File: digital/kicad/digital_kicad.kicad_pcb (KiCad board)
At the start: 2 copper layers, 93 x 49.5 mm, 23 parts, among them J1 Barrel_Jack_Switch, J2 Screw_Terminal_01x02, Q1 2N3904, Q2 2N3904, Q3 FDN340P, Q4 2N3904, SW1 SW_SPST

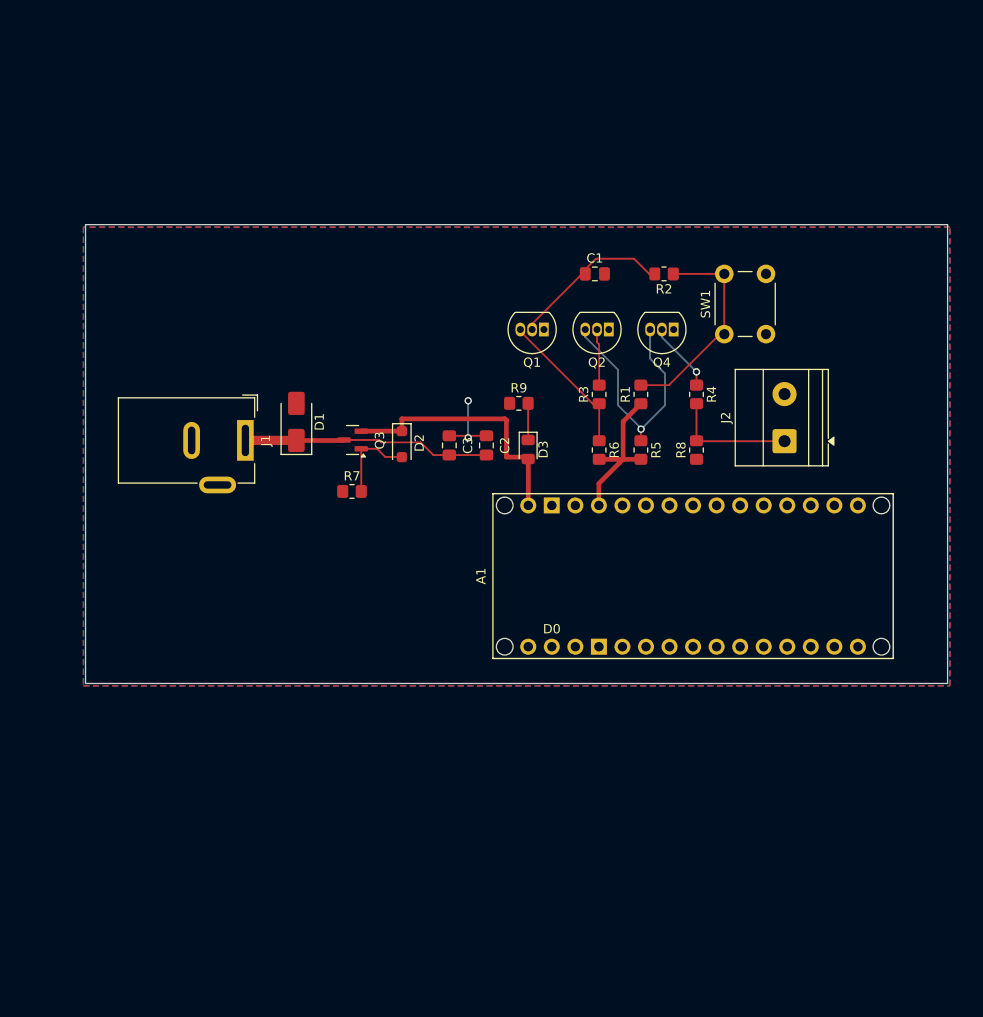
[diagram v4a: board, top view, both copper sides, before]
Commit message: redid the digital schematic to be more compact
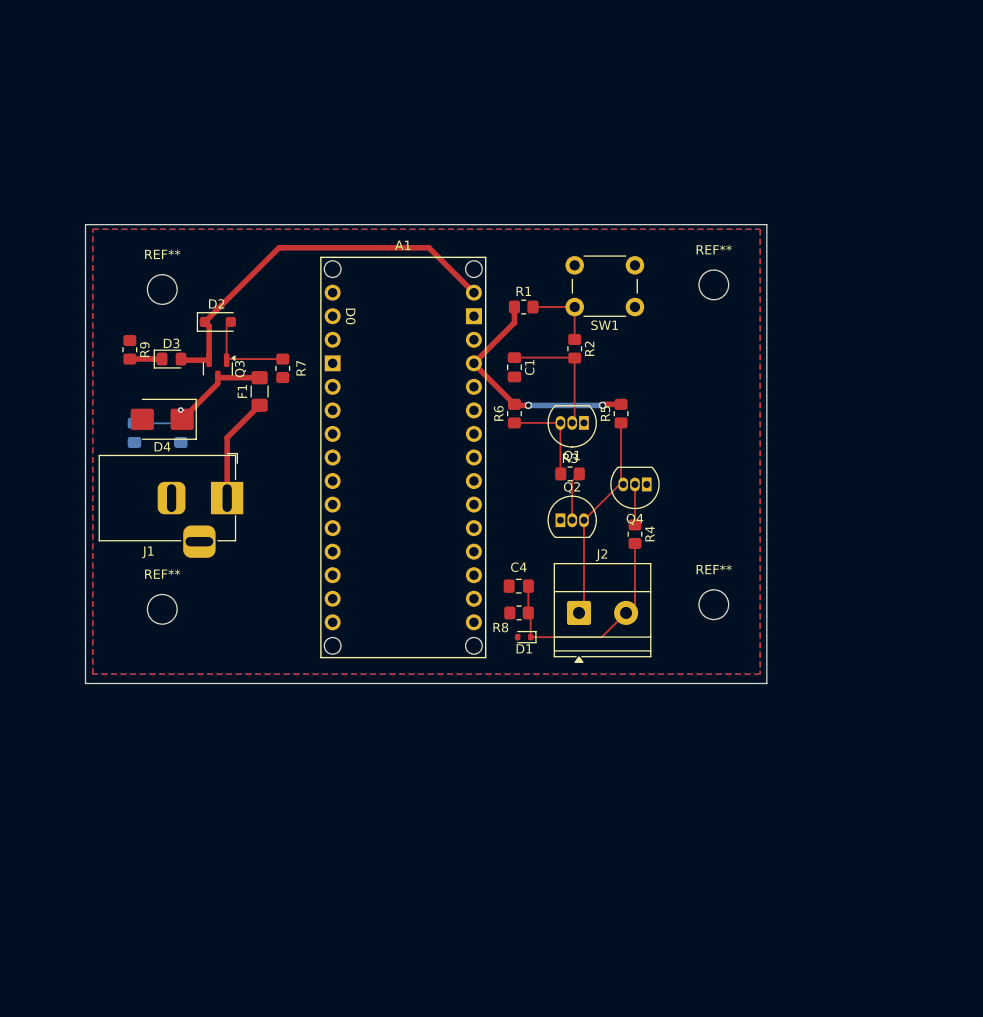
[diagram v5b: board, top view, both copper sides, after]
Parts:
- added C4: 1u, Capacitor_SMD:C_0805_2012Metric_Pad1.18x1.45mm_HandSolder, F.Cu at (152.0, 84.5)
- added D4: SM6T18A, Diode_SMD:D_SMB, F.Cu at (113.5, 66.5)
- added F1: Polyfuse, Fuse:Fuse_1206_3216Metric_Pad1.42x1.75mm_HandSolder, F.Cu at (124.0, 63.5)
- added REF**: MountingHole_3.2mm_M3_DIN965, MountingHole:MountingHole_3.2mm_M3_DIN965, F.Cu at (113.5, 87.0)
- added REF**: MountingHole_3.2mm_M3_DIN965, MountingHole:MountingHole_3.2mm_M3_DIN965, F.Cu at (113.5, 52.5)
- added REF**: MountingHole_3.2mm_M3_DIN965, MountingHole:MountingHole_3.2mm_M3_DIN965, F.Cu at (173.0, 52.0)
- added REF**: MountingHole_3.2mm_M3_DIN965, MountingHole:MountingHole_3.2mm_M3_DIN965, F.Cu at (173.0, 86.5)
- C2, C3: moved to B.Cu
- D1: value SMAJ13A -> ESD5Zxx; footprint Diode_SMD:D_SMA -> Diode_SMD:D_SOD-523
- J1: footprint Connector_BarrelJack:BarrelJack_Wuerth_6941xx301002 -> Connector_BarrelJack:BarrelJack_Horizontal
- R7: value 100k -> 10k
- moved A1 53.6 mm to (139.5, 92.2), turned to 0 degrees
- moved R9 42.4 mm to (110.0, 59.0), turned to -90 degrees
- moved D3 39.7 mm to (114.5, 60.0), turned to 0 degrees
- moved C3 34.0 mm to (110.5, 68.0), turned to -90 degrees
- moved D1 33.8 mm to (152.5, 90.0), turned to 180 degrees
- moved C2 33.0 mm to (115.5, 68.0), turned to -90 degrees
- moved J2 28.9 mm to (158.5, 87.4), turned to 0 degrees
- moved R8 26.0 mm to (152.0, 87.4), turned to 0 degrees
- moved D2 23.8 mm to (119.5, 56.0), turned to 0 degrees
- moved Q2 21.2 mm to (156.5, 77.4), turned to 0 degrees
- moved Q4 17.0 mm to (165.8, 73.5)
- moved R4 16.5 mm to (164.5, 78.9)
- moved Q3 16.4 mm to (119.5, 61.1), turned to -90 degrees
- moved R1 15.8 mm to (152.5, 54.4), turned to 0 degrees
- moved R7 15.2 mm to (126.5, 61.0), turned to 90 degrees
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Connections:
- C2 pad 1: Net-(D1-A1) -> Net-(D4-A1)
- C3 pad 1: Net-(D1-A1) -> Net-(D4-A1)
- D1 pad 1: Net-(D1-A1) -> /DIG_IN
- J1 pad 1: Net-(D1-A1) -> Net-(F1-Pad1)
- J2 pad 1: /DIG_IN -> /OUT
- J2 pad 2: unconnected-(J2-Pin_2-Pad2) -> /DIG_IN
- Q3 pad 3: Net-(D1-A1) -> Net-(D4-A1)
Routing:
- net Net-(D1-A1): track 26.7 -> 0.00 mm
- net Net-(D4-A1): track 0.00 -> 18.1 mm, vias 0 -> 1
- net /SW: track 23.3 -> 8.00 mm
- net /VDC: track 28.6 -> 41.7 mm
- net Net-(F1-Pad1): track 0.00 -> 11.5 mm
- net /DIG_IN: track 13.5 -> 24.9 mm
- net +5V: track 17.4 -> 25.7 mm, vias 0 -> 2
- net GND: track 8.18 -> 0.00 mm, vias 2 -> 0
- net /inv. SW: track 15.9 -> 10.5 mm
- net /OUT: track 27.0 -> 22.8 mm, vias 1 -> 0
- net Net-(Q1-B): track 17.7 -> 13.6 mm
- net A: track 7.55 -> 4.36 mm, vias 1 -> 0
- net Net-(D2-A): track 9.35 -> 10.4 mm
- net Net-(Q2-B): track 6.10 -> 5.32 mm
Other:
- board size 93 x 49.5 mm -> 73.5 x 49.5 mm

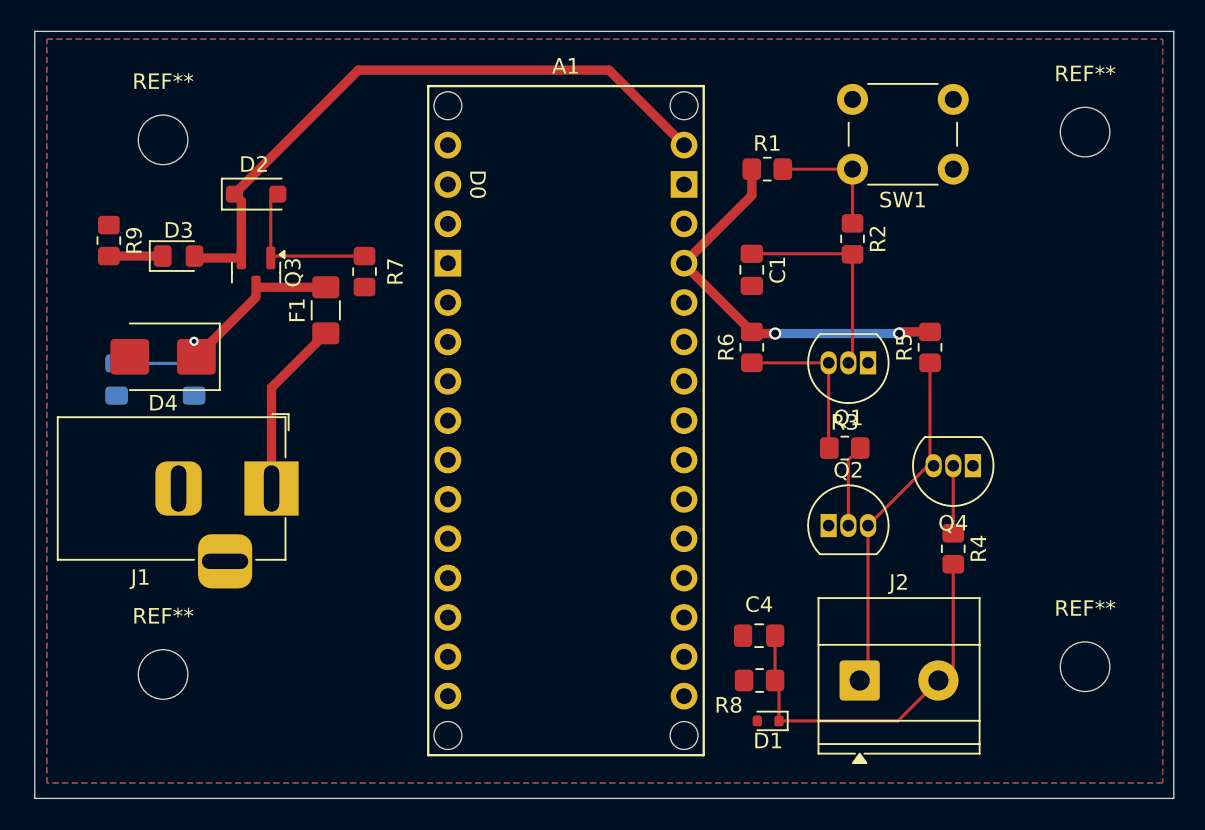
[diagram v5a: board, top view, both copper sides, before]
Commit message: fixed pcb silkscreen, added power switch
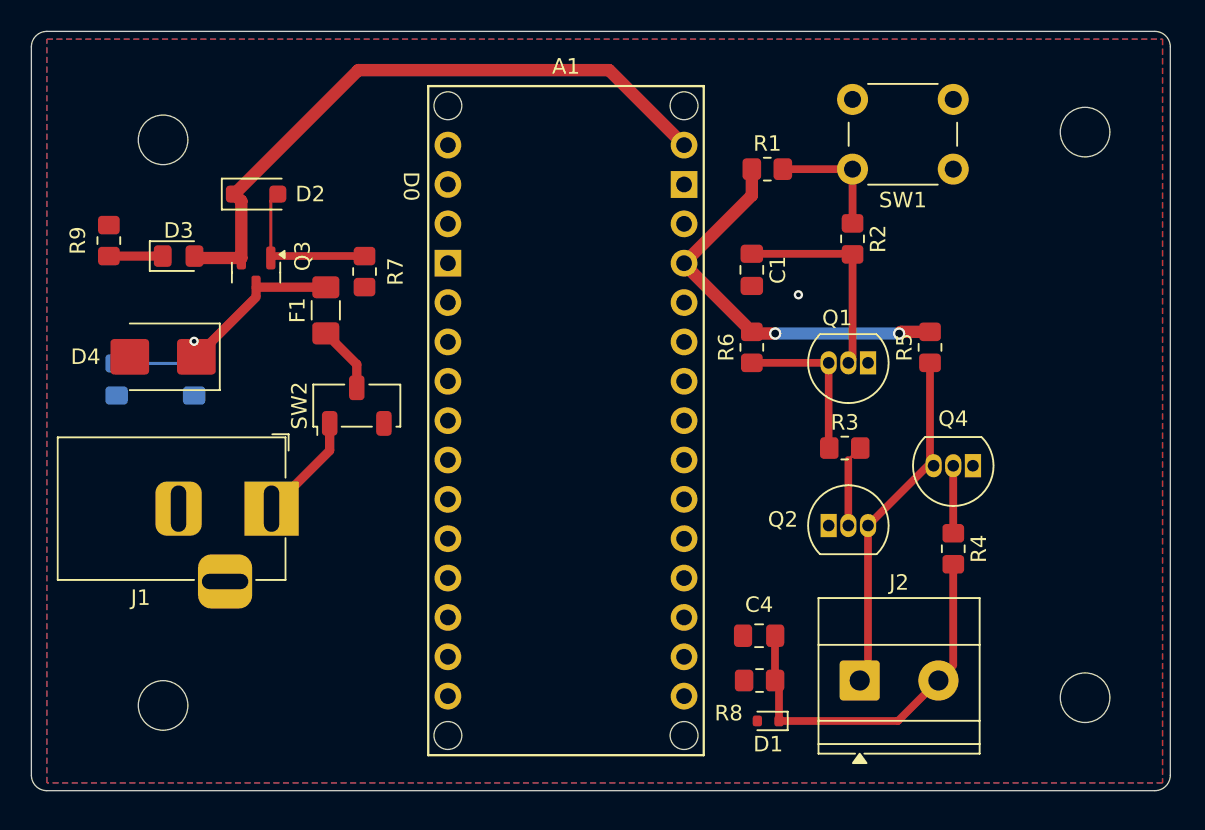
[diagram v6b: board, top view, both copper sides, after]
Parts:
- added SW2: SW_Nidec_CAS-120A1, Button_Switch_SMD:Nidec_Copal_CAS-120A, F.Cu at (126.0, 69.7)
- moved REF** 2.00 mm to (113.5, 89.0)
- moved REF** 2.00 mm to (173.0, 88.5)
- moved J1 1.30 mm to (120.5, 76.3)
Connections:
- F1 pad 1: Net-(F1-Pad1) -> Net-(SW2-B)
- J1 pad 1: Net-(F1-Pad1) -> Net-(SW2-C)
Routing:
- net Net-(F1-Pad1): track 11.5 -> 0.00 mm
- net Net-(SW2-C): track 0.00 -> 7.05 mm
- net Net-(SW2-B): track 0.00 -> 4.34 mm
- net GND: vias 0 -> 1
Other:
- board size 73.5 x 49.5 mm -> 73.5 x 49 mm

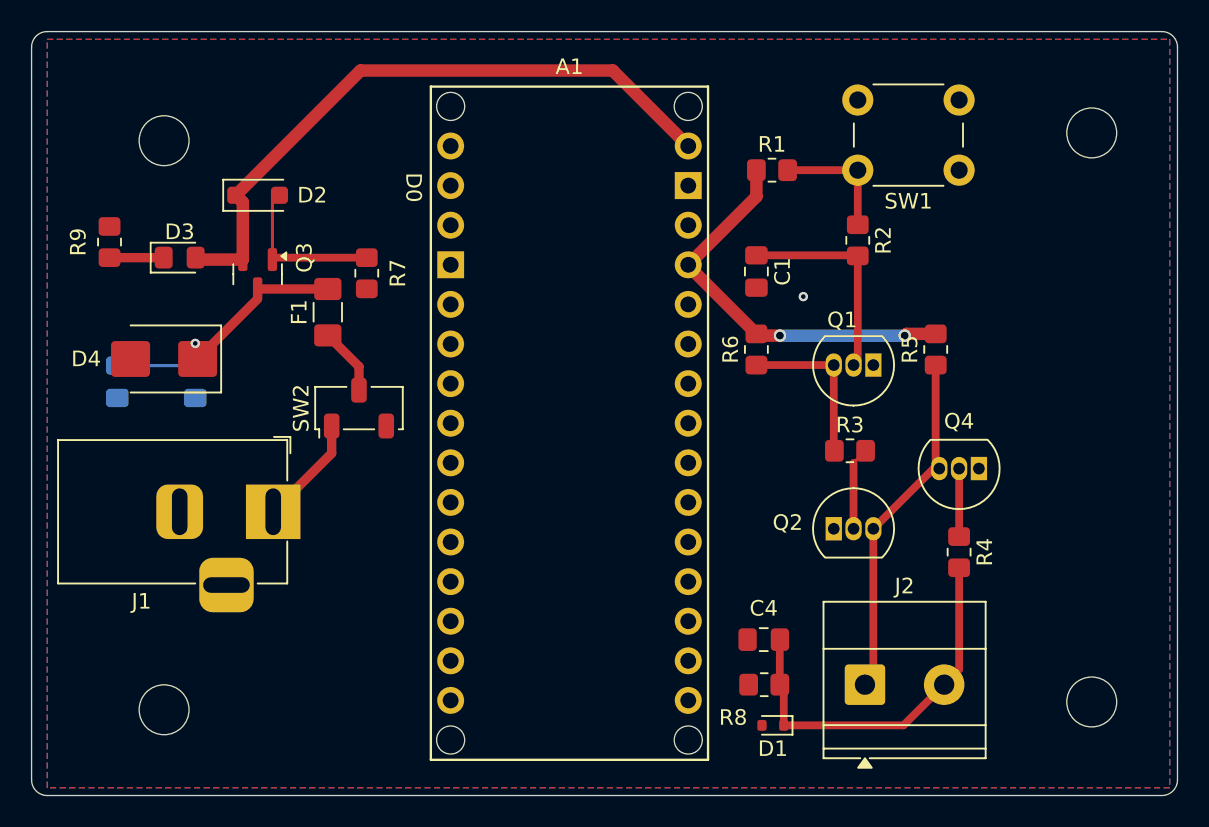
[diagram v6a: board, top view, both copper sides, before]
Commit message: added bigger switch, slightly improved the NOR pcb circuit side track routing
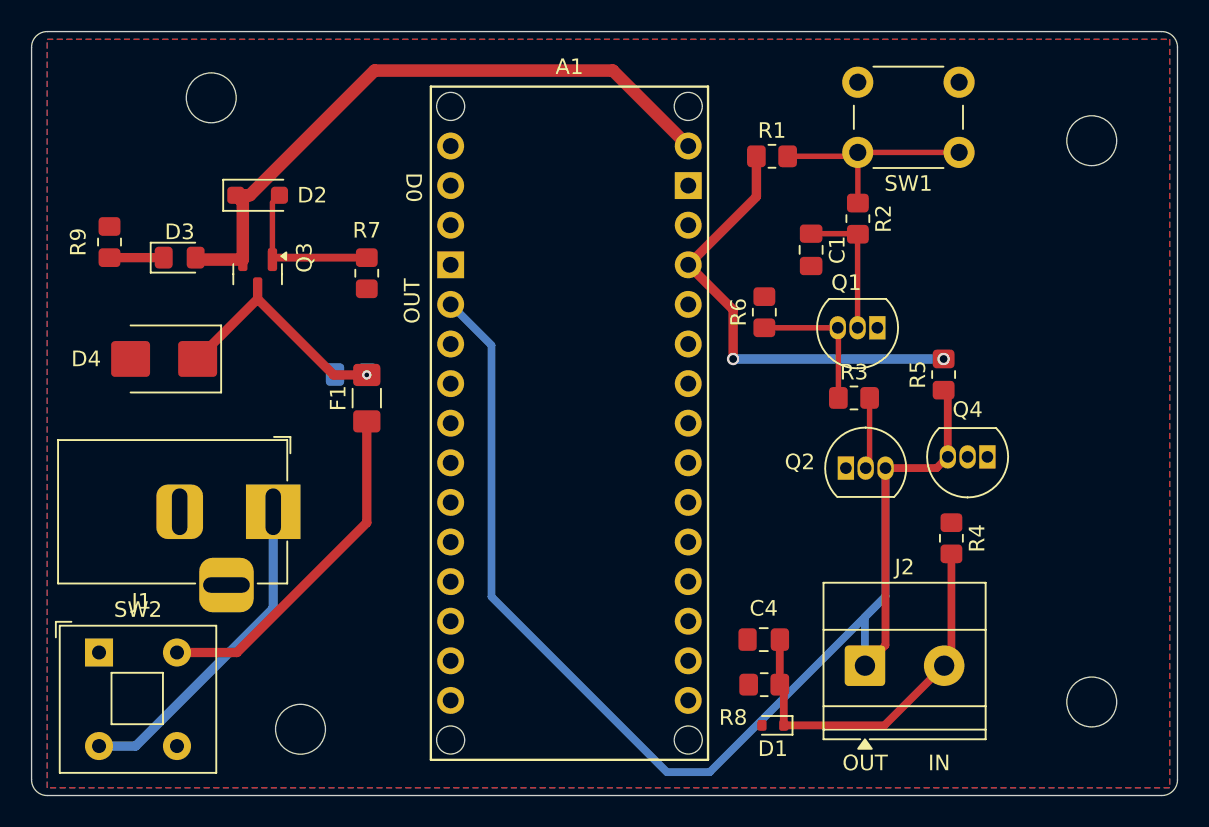
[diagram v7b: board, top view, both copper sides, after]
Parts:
- removed C3: 1u, Capacitor_SMD:C_0805_2012Metric_Pad1.18x1.45mm_HandSolder
- SW2: value SW_Nidec_CAS-120A1 -> SW_Push_SPDT; footprint Button_Switch_SMD:Nidec_Copal_CAS-120A -> Button_Switch_THT:SW_Push_2P1T_Toggle_CK_PVA1xxH1xxxxxxV2
- moved SW2 22.9 mm to (109.3, 85.3), turned to 0 degrees
- moved C2 10.0 mm to (125.5, 67.5), turned to 180 degrees
- moved REF** 8.84 mm to (122.2, 90.2)
- moved F1 6.05 mm to (126.5, 69.0)
- moved REF** 4.09 mm to (116.5, 49.8)
- moved Q2 3.97 mm to (157.2, 73.5)
- moved C1 3.77 mm to (155.0, 59.5)
- moved R3 3.40 mm to (157.8, 69.0)
- moved R6 2.44 mm to (152.0, 63.5)
- moved Q1 2.40 mm to (159.2, 64.5)
- moved R5 1.69 mm to (163.5, 67.5)
- moved R2 1.39 mm to (158.0, 57.5)
- moved J2 1.22 mm to (158.5, 86.2)
- moved SW1 1.14 mm to (164.5, 53.2)
- moved R4 1.02 mm to (164.0, 78.0)
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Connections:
- A1 pad D2: unconnected-(A1-D2_INT0-PadD2) -> /OUT
- SW2 pad 1: Net-(SW2-C) -> GND
- SW2 pad 3: GND -> Net-(SW2-C)
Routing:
- net /OUT: track 22.8 -> 89.2 mm
- net Net-(SW2-B): track 4.34 -> 22.1 mm
- net Net-(SW2-C): track 7.05 -> 21.0 mm
- net /SW: track 8.00 -> 14.0 mm
- net Net-(Q1-B): track 13.6 -> 8.94 mm
- net A: track 4.36 -> 0.00 mm
- net +5V: track 25.7 -> 29.5 mm
- net Net-(D4-A1): track 18.1 -> 15.1 mm
- net /inv. SW: track 10.5 -> 9.17 mm
- net /DIG_IN: track 24.9 -> 23.7 mm
- net Net-(Q2-B): track 5.32 -> 4.25 mm
- net GND: vias 1 -> 0
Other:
- board text added: "IN"
- board text added: "OUT"

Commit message: redid digital schematic to function as adapter, without arduino
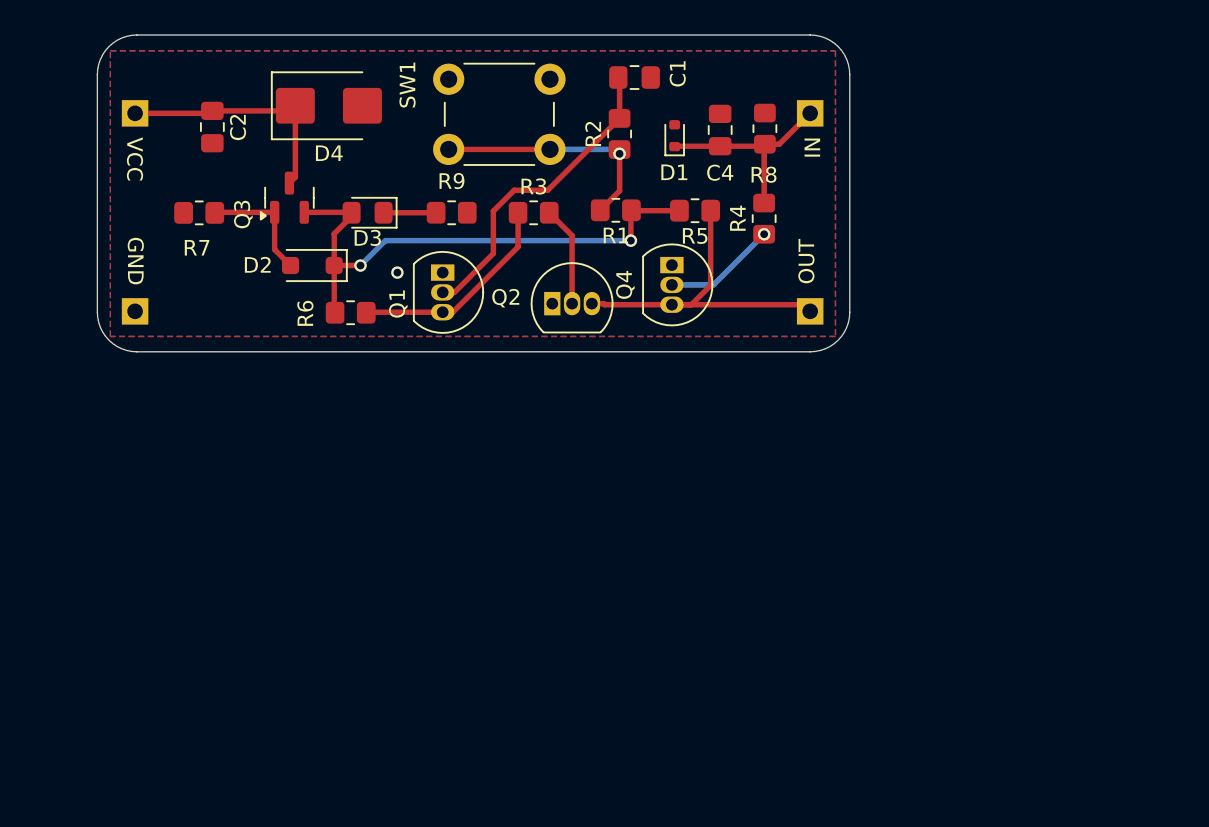
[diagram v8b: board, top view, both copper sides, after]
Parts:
- removed A1: Arduino_Nano_Socket, PCM_arduino-library:Arduino_Nano_Socket
- removed F1: Polyfuse, Fuse:Fuse_1206_3216Metric_Pad1.42x1.75mm_HandSolder
- removed REF** (x4): MountingHole_3.2mm_M3_DIN965, MountingHole:MountingHole_3.2mm_M3_DIN965
- removed SW2: SW_Push_SPDT, Button_Switch_THT:SW_Push_2P1T_Toggle_CK_PVA1xxH1xxxxxxV2
- added J3: Conn_01x01_Pin, Connector_PinHeader_2.54mm:PinHeader_1x01_P2.54mm_Vertical, B.Cu at (154.9, 63.4)
- added J4: Conn_01x01_Pin, Connector_PinHeader_2.54mm:PinHeader_1x01_P2.54mm_Vertical, B.Cu at (154.9, 50.7)
- C2: moved to F.Cu
- J1: value Barrel_Jack_Switch -> Conn_01x01_Pin; footprint Connector_BarrelJack:BarrelJack_Horizontal -> Connector_PinHeader_2.54mm:PinHeader_1x01_P2.54mm_Vertical; moved to B.Cu
- J2: value Screw_Terminal_01x02 -> Conn_01x01_Pin; footprint TerminalBlock_Phoenix:TerminalBlock_Phoenix_MKDS-1,5-2-5.08_1x02_P5.08mm_Horizontal -> Connector_PinHeader_2.54mm:PinHeader_1x01_P2.54mm_Vertical; moved to B.Cu
- R7: value 10k -> 100k
- moved J2 58.7 mm to (111.6, 50.7)
- moved D1 38.3 mm to (146.2, 52.2), turned to 90 degrees
- moved R8 35.7 mm to (152.0, 51.7), turned to -90 degrees
- moved C4 32.8 mm to (149.2, 51.8), turned to 90 degrees
- moved Q1 28.1 mm to (131.4, 61.0), turned to -90 degrees
- moved R6 26.5 mm to (125.5, 63.5), turned to 180 degrees
- moved SW1 26.2 mm to (138.3, 53.1)
- moved R4 23.8 mm to (152.0, 57.5), turned to 90 degrees
- moved R3 23.7 mm to (137.2, 57.1)
- moved Q4 23.7 mm to (146.1, 60.5), turned to -90 degrees
- moved R9 22.0 mm to (131.9, 57.1), turned to 180 degrees
- moved Q2 21.6 mm to (138.4, 63.0)
- moved D4 19.4 mm to (124.1, 50.3), turned to 0 degrees
- moved R5 19.1 mm to (147.6, 57.0), turned to 180 degrees
- moved C2 18.2 mm to (116.6, 51.6), turned to -90 degrees
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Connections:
- net A renamed /A
- C2 pad 1: Net-(D4-A1) -> /DC_IN
- D2 pad 1: /VDC -> +5V
- D3 pad 2: /VDC -> +5V
- D4 pad 1: Net-(D4-A1) -> /DC_IN
- J1 pad 1: Net-(SW2-C) -> GND
- J2 pad 1: /OUT -> /DC_IN
- Q3 pad 2: /VDC -> +5V
- Q3 pad 3: Net-(D4-A1) -> /DC_IN
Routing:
- net /OUT: track 89.2 -> 21.4 mm
- net /VDC: track 41.5 -> 0.00 mm
- net Net-(SW2-B): track 22.1 -> 0.00 mm
- net Net-(SW2-C): track 21.0 -> 0.00 mm
- net Net-(D4-A1): track 15.1 -> 0.00 mm, vias 1 -> 0
- net /DC_IN: track 0.00 -> 14.9 mm
- net Net-(Q1-B): track 8.94 -> 20.1 mm
- net /DIG_IN: track 23.7 -> 13.2 mm
- net /A: track 0.00 -> 7.26 mm, vias 0 -> 1
- net +5V: track 29.5 -> 34.3 mm
- net /inv. SW: track 9.17 -> 13.6 mm
- net Net-(D2-A): track 10.2 -> 7.64 mm
- net Net-(Q2-B): track 4.25 -> 6.43 mm
- net /SW: track 14.0 -> 15.2 mm, vias 0 -> 1
- net GND: vias 0 -> 1
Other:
- board size 73.5 x 49 mm -> 48.3 x 20.3 mm
- board text added: "GND"
- board text added: "VCC"
